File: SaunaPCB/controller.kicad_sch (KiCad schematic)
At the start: 21 parts, among them J301 KL2RM5.08, J302 KL2RM5.08, J303 KL2RM5.08, J304 KL2RM5.08, J305 B2B-ZR, J306 B4B-ZR, J307 B5B-ZR, J308 3-pol-Pfosten, U301 ULN2003, U302 ESP32-DEVKITC

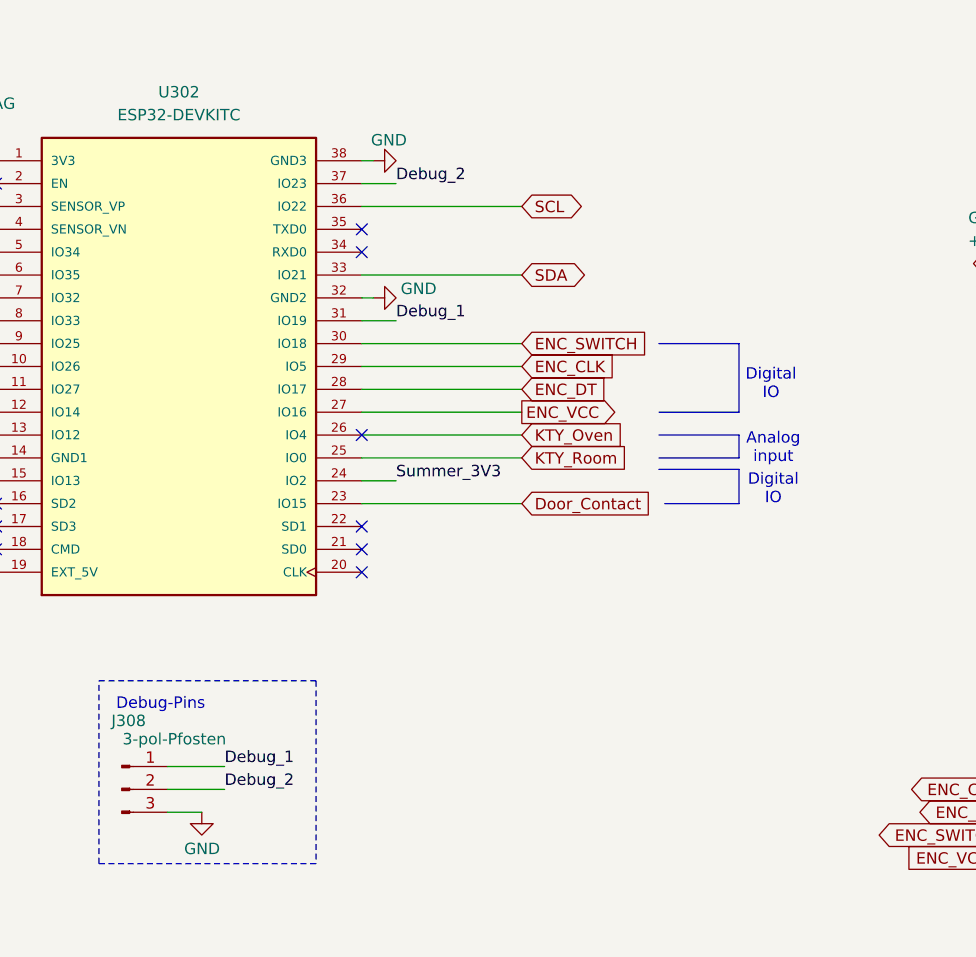
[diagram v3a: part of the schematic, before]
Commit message: Room KTY moved to IO0 (prior buzzer) Buzzer moved to IO23 (prior Debung_2) Debug_2 removed
Reason IO0 does not work properly as ADC input.
Pretty low input impediance...
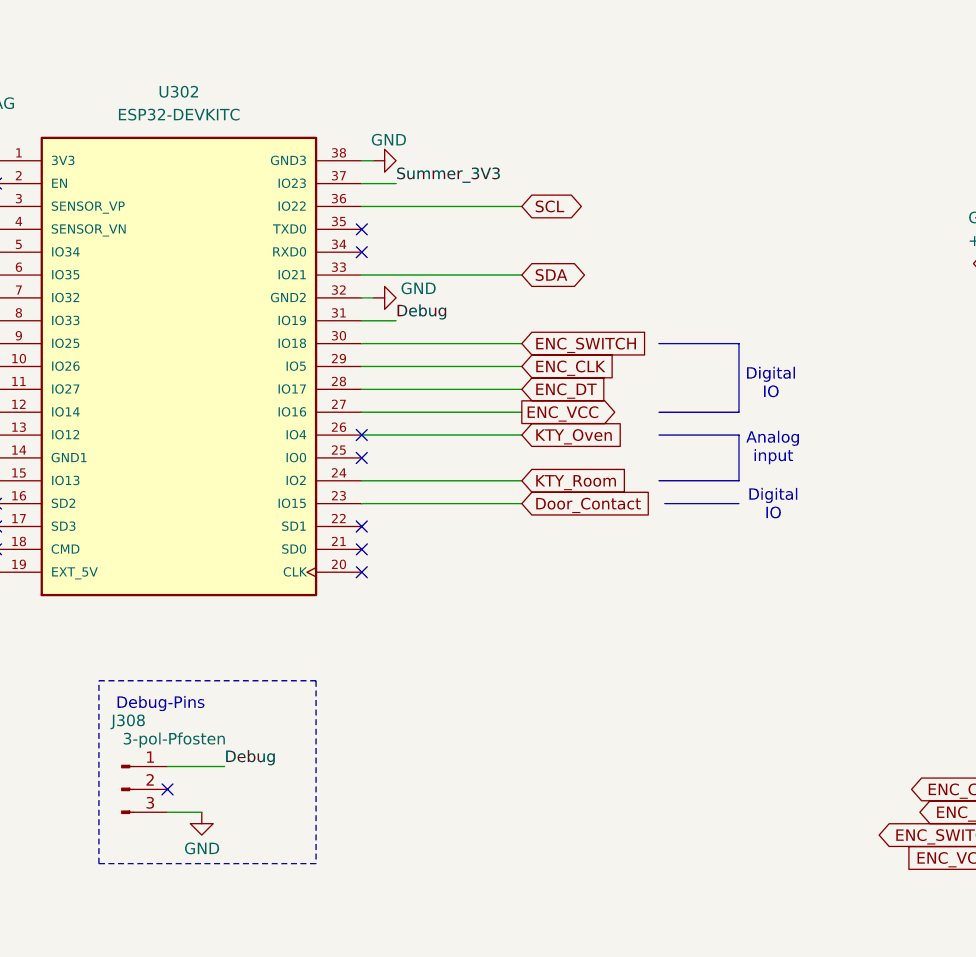
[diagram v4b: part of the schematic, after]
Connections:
- net KTY_Room: now also U302.24 (IO2); no longer U302.25 (IO0)
- net Summer_3V3: now also U302.37 (IO23); no longer U302.24 (IO2)
- net Debug_1 renamed Debug
- net Debug_2: no longer names the net of J308.2 (Pin_2)
- net Debug_2: no longer U302.37 (IO23)
- no-connect marks 10 -> 12
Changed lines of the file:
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@@
 	(text "Digital\nIO"
 		(exclude_from_sim no)
-		(at 213.36 74.676 0)
+		(at 213.36 76.454 0)
 		(effects
 			(font
@@
 	)
 	(no_connect
+		(at 146.05 107.95)
+	)
+	(no_connect
 		(at 167.64 81.28)
+	)
+	(no_connect
+		(at 167.64 71.12)
 	)
 	(no_connect
@@
 	(wire
 		(pts
-			(xy 167.64 71.12) (xy 185.42 71.12)
-		)
-		(stroke
-			(width 0)
-			(type default)
-		)
-	)
-	(wire
-		(pts
 			(xy 254 113.03) (xy 259.08 113.03)
 		)
@@
 	(wire
 		(pts
-			(xy 146.05 107.95) (xy 152.4 107.95)
-		)
-		(stroke
-			(width 0)
-			(type default)
-		)
-	)
-	(wire
-		(pts
 			(xy 76.2 157.48) (xy 78.74 157.48)
 		)
@@
 	(polyline
 		(pts
-			(xy 209.55 68.58) (xy 209.55 71.12)
+			(xy 209.55 68.58) (xy 209.55 73.66)
 		)
 		(stroke
@@
 	(wire
 		(pts
-			(xy 167.64 73.66) (xy 171.45 73.66)
-		)
-		(stroke
-			(width 0)
-			(type default)
-		)
-	)
-	(polyline
-		(pts
-			(xy 200.66 71.12) (xy 209.55 71.12)
+			(xy 167.64 73.66) (xy 185.42 73.66)
+		)
+		(stroke
+			(width 0)
+			(type default)
+		)
+	)
+	(polyline
+		(pts
+			(xy 200.66 73.66) (xy 209.55 73.66)
 		)
 		(stroke
@@
 		)
 	)
-	(polyline
-		(pts
-			(xy 200.66 72.39) (xy 209.55 72.39)
-		)
-		(stroke
-			(width 0)
-			(type default)
-		)
-	)
 	(wire
 		(pts
 			(xy 46.99 64.77) (xy 52.07 64.77)
-		)
-		(stroke
-			(width 0)
-			(type default)
-		)
-	)
-	(polyline
-		(pts
-			(xy 209.55 72.39) (xy 209.55 76.2)
 		)
 		(stroke
@@
 		)
 	)
-	(label "Debug_2"
-		(at 152.4 107.95 0)
-		(effects
-			(font
-				(size 1.27 1.27)
-			)
-			(justify left bottom)
-		)
-	)
 	(label "R2_3V3"
 		(at 111.76 63.5 0)
@@
 		)
 	)
+	(label "Summer_3V3"
+		(at 171.45 40.64 0)
+		(effects
+			(font
+				(size 1.27 1.27)
+			)
+			(justify left bottom)
+		)
+	)
 	(label "R3_3V3"
 		(at 106.68 167.64 0)
@@
 	)
 	(label "Summer_3V3"
-		(at 171.45 73.66 0)
-		(effects
-			(font
-				(size 1.27 1.27)
-			)
-			(justify left bottom)
-		)
-	)
-	(label "Summer_3V3"
 		(at 106.68 172.72 0)
 		(effects
@@
 		)
 	)
-	(label "Debug_2"
-		(at 171.45 40.64 0)
-		(effects
-			(font
-				(size 1.27 1.27)
-			)
-			(justify left bottom)
-		)
-	)
-	(label "Debug_1"
+	(label "Debug"
 		(at 171.45 55.88 0)
 		(effects
@@
 		)
 	)
-	(label "Debug_1"
+	(label "Debug"
 		(at 152.4 105.41 0)
 		(effects
@@
 	(global_label "KTY_Room"
 		(shape input)
-		(at 185.42 71.12 0)
+		(at 185.42 73.66 0)
 		(fields_autoplaced yes)
 		(effects
@@
 		)
 		(property "Intersheetrefs" "${INTERSHEET_REFS}"
-			(at 197.9603 71.12 0)
+			(at 197.9603 73.66 0)
 			(effects
 				(font
